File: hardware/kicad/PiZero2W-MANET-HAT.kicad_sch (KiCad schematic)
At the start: 0 parts

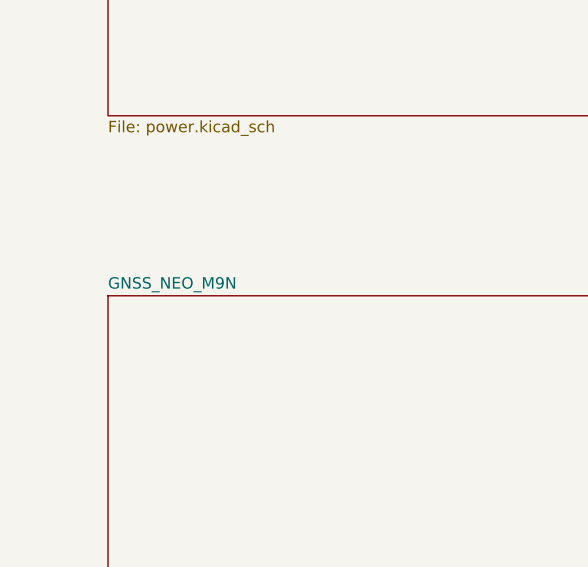
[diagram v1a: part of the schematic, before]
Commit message: Add gap-analysis components (datasheet-grounded) + RTC
Read the uploaded datasheets (MM8108-MF15457, E21-900G30S, NEO-M9N-00B)
and resolved the component gaps:

- #1/#2 RESOLVED by the module: MF15457 is self-contained (internal
  clock+PMU+PA); only needs VBAT/VBAT_TX/VDDIO 3.0-3.6 V. No external SoC
  inductors, 1V8/1V2 rails, or TCXO.
- VPA fixed at 5.0 V (E21 needs 4.75-5.25 V, ~620 mA TX, +20 dBm in ->
  +30 dBm out, 12 dB gain). Real pinouts wired (module 38-pin; E21
  pin6=PIN xcvr, pin9=ANT).
- Architecture finding: module has integrated PA + single ANT pin and NO
  hardware T/R FEM line. External E21 now needs (a) ~3-5 dB drive pad,
  (b) T/R control via module GPIO0/1 toggled by OpenMANET FW (or RF-sense
  auto-T/R fallback), and (c) end-product recertification at +30 dBm.

Added components:
- N3 900 MHz harmonic LPF (FL2); N4 inrush soft-start load switch (U10);
  N5 supervisor (U11); N6 radio-rail load switch (U12, OpenMANET
  power-gpios); N7 RF shields; N8 GNSS antenna ESD (D8); N9 status LEDs;
  N10 E21 thermal relief.
- RTC: RV-3028-C7 (U13) on I2C1 0x52 with a soldered rechargeable cell
  (BT1, trickle-charged) per request; added to the device-tree overlay.
- Declined per request: debug UART/JTAG pads, test points.

Updated docs (new COMPONENTS_GAP.md; DECISIONS B1-B9; SCHEMATIC; BOM;
POWER budget), netlist, overlay, and regenerated the KiCad 10 scaffold
with the new nets. Committed the vendor datasheets under hardware/.

https://claude.ai/code/session_015nkkW85U3sPf5mcvrsMw7T
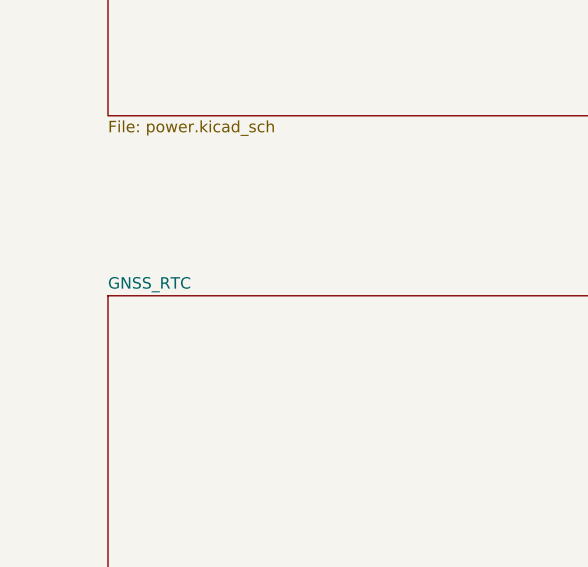
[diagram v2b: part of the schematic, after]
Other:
- removed sheet GNSS_NEO_M9N
- added sheet GNSS_RTC (gnss.kicad_sch)
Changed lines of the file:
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@@
 		(instances
 			(project "PiZero2W-MANET-HAT"
-				(path "/3692a164-a15a-411e-a580-4d3d4c06973b" (page "2"))
+				(path "/8f288caf-94f1-454a-abd6-6df91097e52e" (page "2"))
 			)
 		)
@@
 		(instances
 			(project "PiZero2W-MANET-HAT"
-				(path "/3692a164-a15a-411e-a580-4d3d4c06973b" (page "3"))
+				(path "/8f288caf-94f1-454a-abd6-6df91097e52e" (page "3"))
 			)
 		)
@@
 		(instances
 			(project "PiZero2W-MANET-HAT"
-				(path "/3692a164-a15a-411e-a580-4d3d4c06973b" (page "4"))
+				(path "/8f288caf-94f1-454a-abd6-6df91097e52e" (page "4"))
 			)
 		)
@@
 		(stroke (width 0.1524) (type solid))
 		(fill (color 0 0 0 0.0000))
-		(property "Sheetname" "GNSS_NEO_M9N" (at 30 94.36 0) (effects (font (size 1.27 1.27)) (justify left bottom)))
+		(property "Sheetname" "GNSS_RTC" (at 30 94.36 0) (effects (font (size 1.27 1.27)) (justify left bottom)))
 		(property "Sheetfile" "gnss.kicad_sch" (at 30 130.5 0) (effects (font (size 1.27 1.27)) (justify left top)))
 		(instances
 			(project "PiZero2W-MANET-HAT"
-				(path "/3692a164-a15a-411e-a580-4d3d4c06973b" (page "5"))
+				(path "/8f288caf-94f1-454a-abd6-6df91097e52e" (page "5"))
 			)
 		)
@@
 		(instances
 			(project "PiZero2W-MANET-HAT"
-				(path "/3692a164-a15a-411e-a580-4d3d4c06973b" (page "6"))
+				(path "/8f288caf-94f1-454a-abd6-6df91097e52e" (page "6"))
 			)
 		)

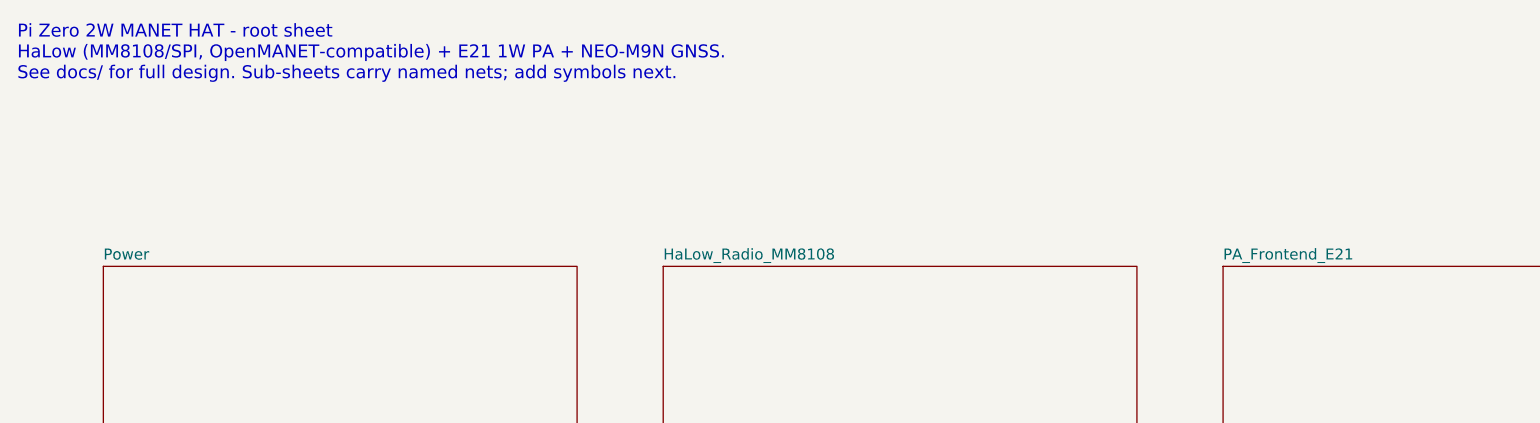
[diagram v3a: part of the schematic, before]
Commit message: Pivot to MM8108-M20 primary / MF15457 fallback; retire external E21
Per the decision to make the MM8108-M20 the primary radio (with MF15457
as the build-today fallback) and retire the external E21 PA path:

Design:
- One radio site fed by the shared SPI/control nets accepts either module.
- Removed the E21 PA, 5V buck-boost (VPA), harmonic LPF, drive pad, T/R
  control, RF-sense VOX, and RF bypass. Both modules drive the antenna
  directly (M20 = integrated 28.5 dBm PA + 902-928 SAW, certified;
  MF15457 = ~27 dBm). Power collapses to a single 3V3 rail.
- Header GPIO4/6 (old FEM fallback) revert to spares; GPIO12/13 drive the
  status LEDs.
- M20 pinout/power/footprint held at placeholder pending its datasheet
  (B12); MF15457 pin-level detail stays the concrete baseline.

Docs updated: DECISIONS (A3 superseded, B11/B12 added, B2-B5/B10 retired,
new radio-options table + order), DESIGN, SCHEMATIC, POWER, RF, BOM,
INTERFACES, COMPONENTS_GAP, LINK_BUDGET, FIRMWARE_PA, BRINGUP, MECHANICAL,
README. Netlist, KiCad scaffold (sheets/silk/root note), and the OpenMANET
overlay/README updated to match. Scaffold regenerated and validated.

https://claude.ai/code/session_015nkkW85U3sPf5mcvrsMw7T
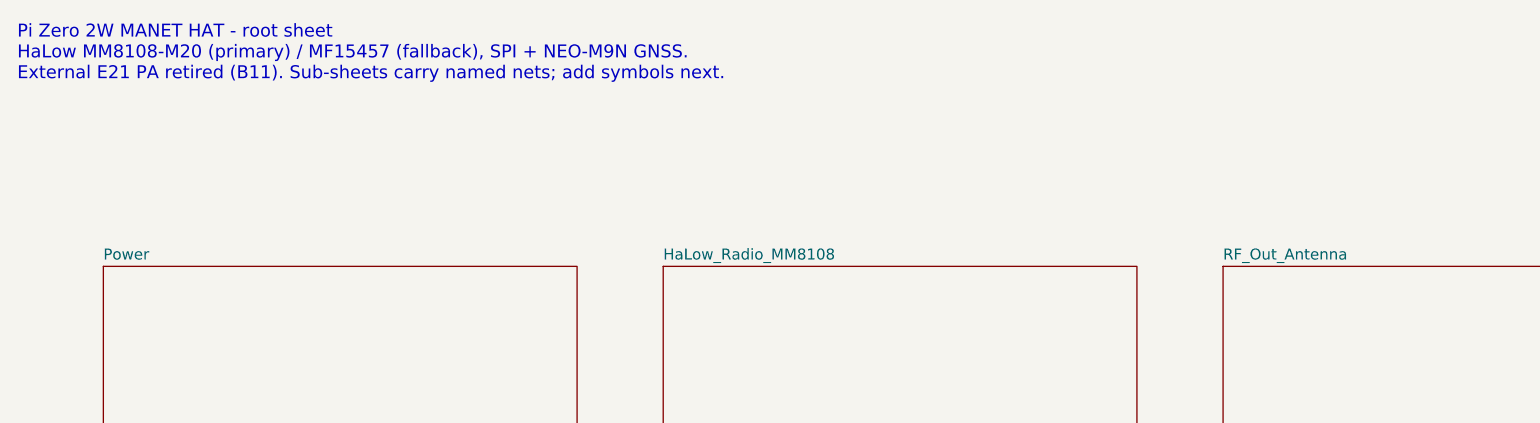
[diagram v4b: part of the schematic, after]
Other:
- removed sheet PA_Frontend_E21
- added sheet RF_Out_Antenna (pa_frontend.kicad_sch)
- note added: "Pi Zero 2W MANET HAT - root sheet HaLow MM8108-M20 (primary) / MF15457 (fallback), SPI + NEO-M9N GNSS. External E21 PA retired (B11). Sub-sheets carry named nets; add symbols next."
- note removed: "Pi Zero 2W MANET HAT - root sheet HaLow (MM8108/SPI, OpenMANET-compatible) + E21 1W PA + NEO-M9N GNSS. See docs/ for full design. Sub-sheets carry named nets; add symbols next."
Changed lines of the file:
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@@
 	(generator_version "10.0")
 	(paper "A4")
-	(text "Pi Zero 2W MANET HAT - root sheet\nHaLow (MM8108/SPI, OpenMANET-compatible) + E21 1W PA + NEO-M9N GNSS.\nSee docs/ for full design. Sub-sheets carry named nets; add symbols next." (exclude_from_sim no) (at 20 12 0) (effects (font (size 1.5 1.5)) (justify left top)))
+	(text "Pi Zero 2W MANET HAT - root sheet\nHaLow MM8108-M20 (primary) / MF15457 (fallback), SPI + NEO-M9N GNSS.\nExternal E21 PA retired (B11). Sub-sheets carry named nets; add symbols next." (exclude_from_sim no) (at 20 12 0) (effects (font (size 1.5 1.5)) (justify left top)))
 	(sheet
 		(at 30 40)
@@
 		(instances
 			(project "PiZero2W-MANET-HAT"
-				(path "/43aba5d6-287a-403e-b882-7bbb3efed6d8" (page "2"))
+				(path "/68fac97a-3676-4757-ad4a-dceea239e277" (page "2"))
 			)
 		)
@@
 		(instances
 			(project "PiZero2W-MANET-HAT"
-				(path "/43aba5d6-287a-403e-b882-7bbb3efed6d8" (page "3"))
+				(path "/68fac97a-3676-4757-ad4a-dceea239e277" (page "3"))
 			)
 		)
@@
 		(stroke (width 0.1524) (type solid))
 		(fill (color 0 0 0 0.0000))
-		(property "Sheetname" "PA_Frontend_E21" (at 160 39.36 0) (effects (font (size 1.27 1.27)) (justify left bottom)))
+		(property "Sheetname" "RF_Out_Antenna" (at 160 39.36 0) (effects (font (size 1.27 1.27)) (justify left bottom)))
 		(property "Sheetfile" "pa_frontend.kicad_sch" (at 160 75.5 0) (effects (font (size 1.27 1.27)) (justify left top)))
 		(instances
 			(project "PiZero2W-MANET-HAT"
-				(path "/43aba5d6-287a-403e-b882-7bbb3efed6d8" (page "4"))
+				(path "/68fac97a-3676-4757-ad4a-dceea239e277" (page "4"))
 			)
 		)
@@
 		(instances
 			(project "PiZero2W-MANET-HAT"
-				(path "/43aba5d6-287a-403e-b882-7bbb3efed6d8" (page "5"))
+				(path "/68fac97a-3676-4757-ad4a-dceea239e277" (page "5"))
 			)
 		)
@@
 		(instances
 			(project "PiZero2W-MANET-HAT"
-				(path "/43aba5d6-287a-403e-b882-7bbb3efed6d8" (page "6"))
+				(path "/68fac97a-3676-4757-ad4a-dceea239e277" (page "6"))
 			)
 		)
